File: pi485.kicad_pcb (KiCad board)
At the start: 2 copper layers, 45 x 52 mm, 22 parts, among them J1 RS485, P1 Rasperry Pi, P2 PWR, P3 Term, Q1 NPN, U1 NE555, U2 MAX485

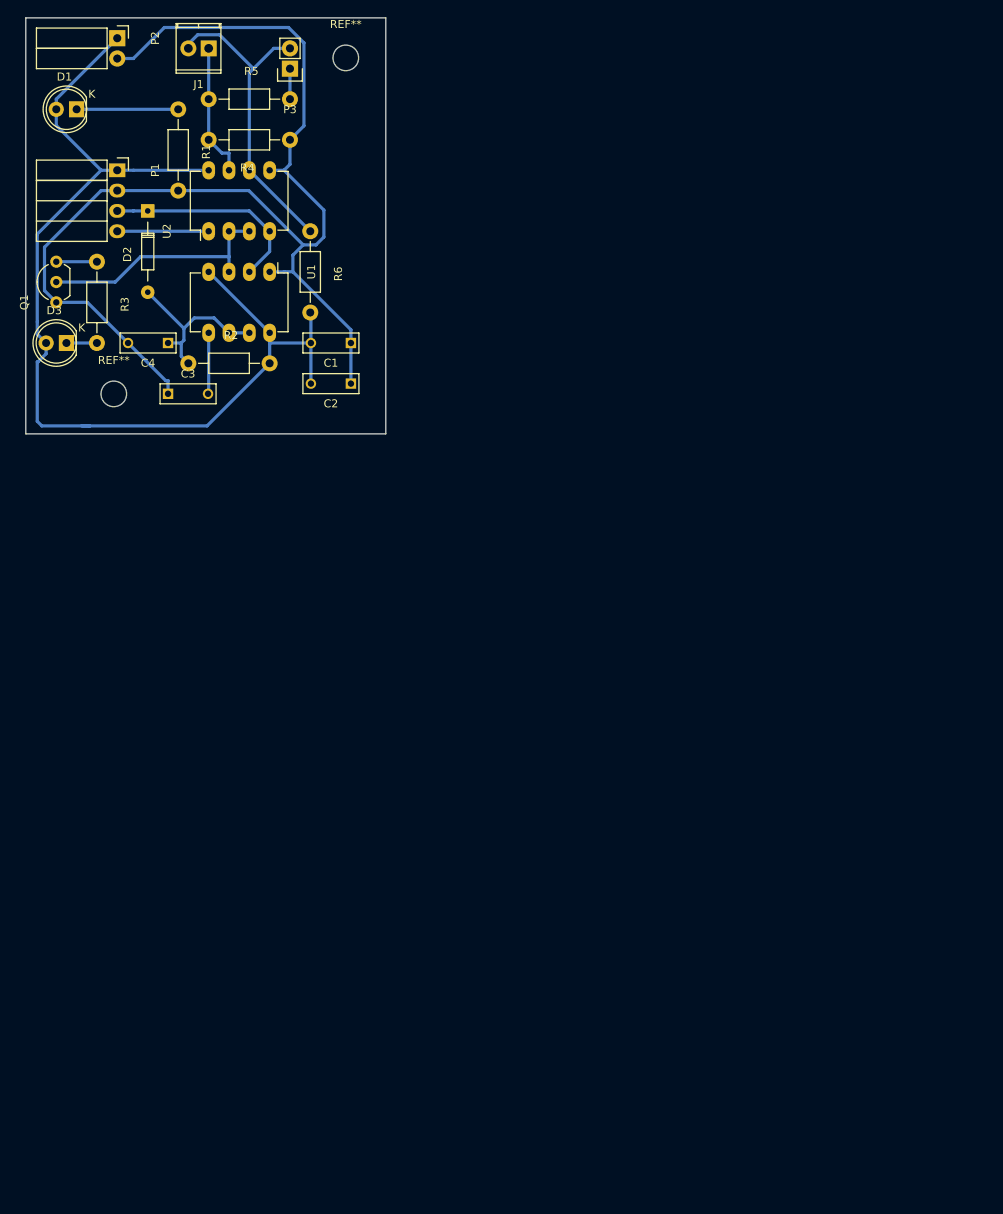
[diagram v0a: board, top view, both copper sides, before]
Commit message: Made a bunch of changes...
New board size (70mm x 53mm) single layer, better layout.
Replace silicon diode with saturated NPN, added NPN tirggered TX / RX LEDs.
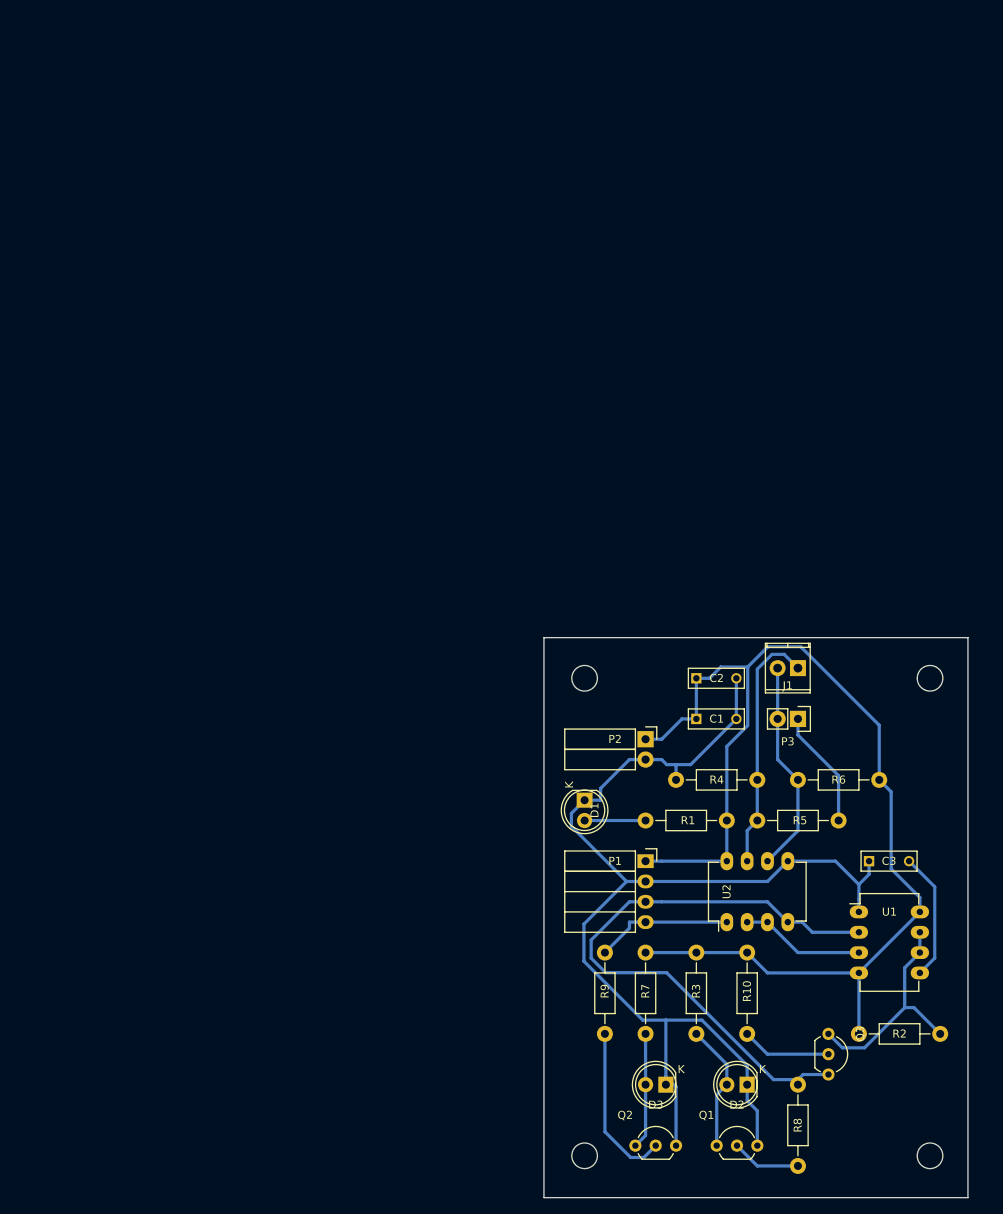
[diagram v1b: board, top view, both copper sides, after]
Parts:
- removed C4: 10nF, Capacitors_THT:C_Rect_L7_W2.5_P5
- removed REF** (x2): MountingHole_3.2mm_M3, Mounting_Holes:MountingHole_3.2mm_M3
- added Q2: 2N4401, TO_SOT_Packages_THT:TO-92_Inline_Wide, F.Cu at (88.1, 153.0)
- added Q3: 2N4401, TO_SOT_Packages_THT:TO-92_Inline_Wide, F.Cu at (112.3, 139.1)
- added R10: 2.5k, Resistors_THT:Resistor_Horizontal_RM10mm, F.Cu at (102.1, 139.1)
- added R7: 220, Resistors_THT:Resistor_Horizontal_RM10mm, F.Cu at (89.4, 139.1)
- added R8: 2.5k, Resistors_THT:Resistor_Horizontal_RM10mm, F.Cu at (108.5, 155.6)
- added R9: 2.5k, Resistors_THT:Resistor_Horizontal_RM10mm, F.Cu at (84.3, 139.1)
- added REF01: MountingHole_3.2mm_M3, Mounting_Holes:MountingHole_3.2mm_M3, F.Cu at (81.8, 94.6)
- added REF02: MountingHole_3.2mm_M3, Mounting_Holes:MountingHole_3.2mm_M3, F.Cu at (125.0, 94.6)
- added REF03: MountingHole_3.2mm_M3, Mounting_Holes:MountingHole_3.2mm_M3, F.Cu at (125.0, 154.3)
- added REF04: MountingHole_3.2mm_M3, Mounting_Holes:MountingHole_3.2mm_M3, F.Cu at (81.8, 154.3)
- C1: value 0.1uF -> 10uF
- C2: value 10uF -> 0.1uF
- D2: value BAT43 -> TX; footprint Diodes_THT:Diode_DO-35_SOD27_Horizontal_RM10 -> LEDs:LED-5MM
- D3: value TX -> RX
- Q1: value NPN -> 2N4401
- R3: value 470 -> 220
- moved Q1 133.9 mm to (98.3, 153.0), turned to 0 degrees
- moved D2 132.5 mm to (102.1, 145.4), turned to 180 degrees
- moved R2 125.9 mm to (126.2, 139.1), turned to 180 degrees
- moved R3 122.2 mm to (95.8, 139.1), turned to 90 degrees
- moved D3 119.2 mm to (91.9, 145.4)
- moved R5 113.3 mm to (103.4, 112.4)
- moved R1 112.3 mm to (99.6, 112.4), turned to 180 degrees
- moved P2 109.7 mm to (89.4, 102.2)
- moved U1 108.8 mm to (116.1, 123.8), turned to 0 degrees
- moved P1 108.7 mm to (89.4, 117.5)
- moved U2 108.0 mm to (99.6, 125.1)
- moved D1 107.2 mm to (81.8, 109.9), turned to 270 degrees
- moved J1 106.9 mm to (108.5, 93.3)
- moved C3 105.3 mm to (117.3, 117.5)
- moved P3 103.1 mm to (108.5, 99.7), turned to 270 degrees
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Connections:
- C1 pad 1: GND -> VCC
- C1 pad 2: VCC -> GND
- C2 pad 1: GND -> VCC
- C2 pad 2: VCC -> GND
- D1 pad 1: Net-(D1-Pad1) -> GND
- D1 pad 2: VCC -> Net-(D1-Pad2)
- D2 pad 1: /(TXDO)_GPIO14 -> GND
- D2 pad 2: Net-(C4-Pad1) -> Net-(D2-Pad2)
- D3 pad 1: Net-(D3-Pad1) -> GND
- D3 pad 2: VCC -> Net-(D3-Pad2)
- Q1 pad 1: GND -> Net-(D2-Pad2)
- Q1 pad 3: Net-(Q1-Pad3) -> GND
- R1 pad 1: Net-(D1-Pad1) -> VCC
- R1 pad 2: GND -> Net-(D1-Pad2)
- R2 pad 1: Net-(C4-Pad1) -> Net-(Q3-Pad1)
- R3 pad 1: Net-(Q1-Pad3) -> Net-(D2-Pad2)
- R3 pad 2: Net-(D3-Pad1) -> VCC
- U1 pad 3: Net-(Q1-Pad2) -> Net-(U1-Pad3)
- U1 pad 6: Net-(C4-Pad1) -> Net-(Q3-Pad1)
- U1 pad 7: Net-(C4-Pad1) -> Net-(Q3-Pad1)
- U2 pad 2: Net-(Q1-Pad2) -> Net-(U1-Pad3)
- U2 pad 3: Net-(Q1-Pad2) -> Net-(U1-Pad3)
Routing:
- net /(TXDO)_GPIO14: track 26.2 -> 76.1 mm
- net Net-(Q3-Pad1): track 0.00 -> 28.3 mm
- net Net-(C4-Pad1): track 22.4 -> 0.00 mm
- net Net-(Q1-Pad2): track 30.5 -> 8.67 mm
- net Net-(Q2-Pad2): track 0.00 -> 20.5 mm
- net Net-(D2-Pad2): track 0.00 -> 16.1 mm
- net Net-(U1-Pad3): track 0.00 -> 15.5 mm
- net VCC: track 133.3 -> 148.1 mm
- net Net-(D3-Pad2): track 0.00 -> 14.5 mm
- net Net-(J1-Pad1): track 16.8 -> 31.1 mm
- net Net-(J1-Pad2): track 40.2 -> 26.8 mm
- net Net-(D1-Pad1): track 12.7 -> 0.00 mm
- net Net-(Q3-Pad2): track 0.00 -> 11.2 mm
- net Net-(P3-Pad1): track 3.81 -> 14.8 mm
- net Net-(C3-Pad2): track 7.65 -> 16.1 mm
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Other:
- board size 45 x 52 mm -> 53 x 70 mm

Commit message: Updating...
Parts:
- D1: value PWR -> PWRLED
- D2: value TX -> TXLED
- D3: value RX -> RXLED
- Q1, Q2, Q3: value 2N4401 -> 2N2222
- R1, R10, R2, R3, R4, R5, R6, R7, R9: footprint Resistors_THT:Resistor_Horizontal_RM10mm -> Resistors_THT:Resistor_Horizontal_RM7mm
- R8: footprint Resistors_THT:Resistor_Horizontal_RM10mm -> Resistors_THT:Resistor_Horizontal_RM15mm
- moved R8 42.8 mm to (109.2, 112.8)
- moved Q1 35.9 mm to (106.7, 118.1)
- moved Q2 35.9 mm to (96.5, 118.1)
- moved Q3 35.6 mm to (127.0, 106.7), turned to 180 degrees
- moved C1 33.8 mm to (99.1, 66.0), turned to 180 degrees
- moved C2 33.8 mm to (99.0, 61.0), turned to 180 degrees
- moved R4 33.2 mm to (100.3, 74.9)
- moved R5 33.2 mm to (110.5, 80.0)
- moved R6 33.2 mm to (115.6, 74.9)
- moved C3 32.7 mm to (121.9, 85.1)
- moved R1 32.7 mm to (104.1, 80.0)
- moved REF01 32.2 mm to (88.0, 63.0)
- moved REF02 31.8 mm to (128.0, 63.0)
- moved U1 31.4 mm to (120.7, 92.7)
- moved P1 31.4 mm to (94.0, 86.4)
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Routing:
- net /(TXDO)_GPIO14: track 76.1 -> 88.6 mm
- net Net-(Q2-Pad2): track 20.5 -> 8.45 mm
- net GND: track 149.2 -> 160.8 mm
- net Net-(Q3-Pad2): track 11.2 -> 22.5 mm
- net VCC: track 148.1 -> 156.5 mm
- net Net-(U1-Pad3): track 15.5 -> 22.4 mm
- net Net-(D3-Pad2): track 14.5 -> 18.4 mm
- net Net-(D1-Pad2): track 7.62 -> 3.81 mm
- net Net-(Q1-Pad2): track 8.67 -> 5.32 mm
- net /(RXDO)_GPIO15: track 17.3 -> 20.3 mm
- net Net-(J1-Pad1): track 31.1 -> 33.8 mm
- net Net-(D2-Pad2): track 16.1 -> 18.4 mm
- net Net-(P3-Pad1): track 14.8 -> 12.8 mm
- net Net-(C3-Pad2): track 16.1 -> 17.9 mm
- net Net-(Q3-Pad1): track 28.3 -> 29.5 mm
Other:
- board size 53 x 70 mm -> 48 x 70 mm
- net class Default: clearance 0.5 -> 0.75; trace_width 0.4 -> 0.75; via_dia 0.8 -> 1.2; via_drill 0.4 -> 0.8
- rule pad_to_mask_clearance: 1 -> 0
- rule trace_clearance: 0.5 -> 0.75
- rule trace_min: 0.4 -> 0.75
- rule via_min_drill: 0.3 -> 0.8
- rule via_min_size: 0.8 -> 1.2
- board text added: "+5vDC"
- board text added: "GND"
- board text added: "Pi485 Rev 1.0.0 2017-1-12"
- board text added: "UART RX"
- board text added: "UART TX"
